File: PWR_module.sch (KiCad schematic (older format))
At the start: 16 parts, among them P14 CONN_01X02, P15 FUSE, T1 TRANSFO, U1 SPX2920M3-3.3, U7 SPX2920M3-3.3, U8 SPX2920M3-3.3, U9 SPX2920M3-3.3

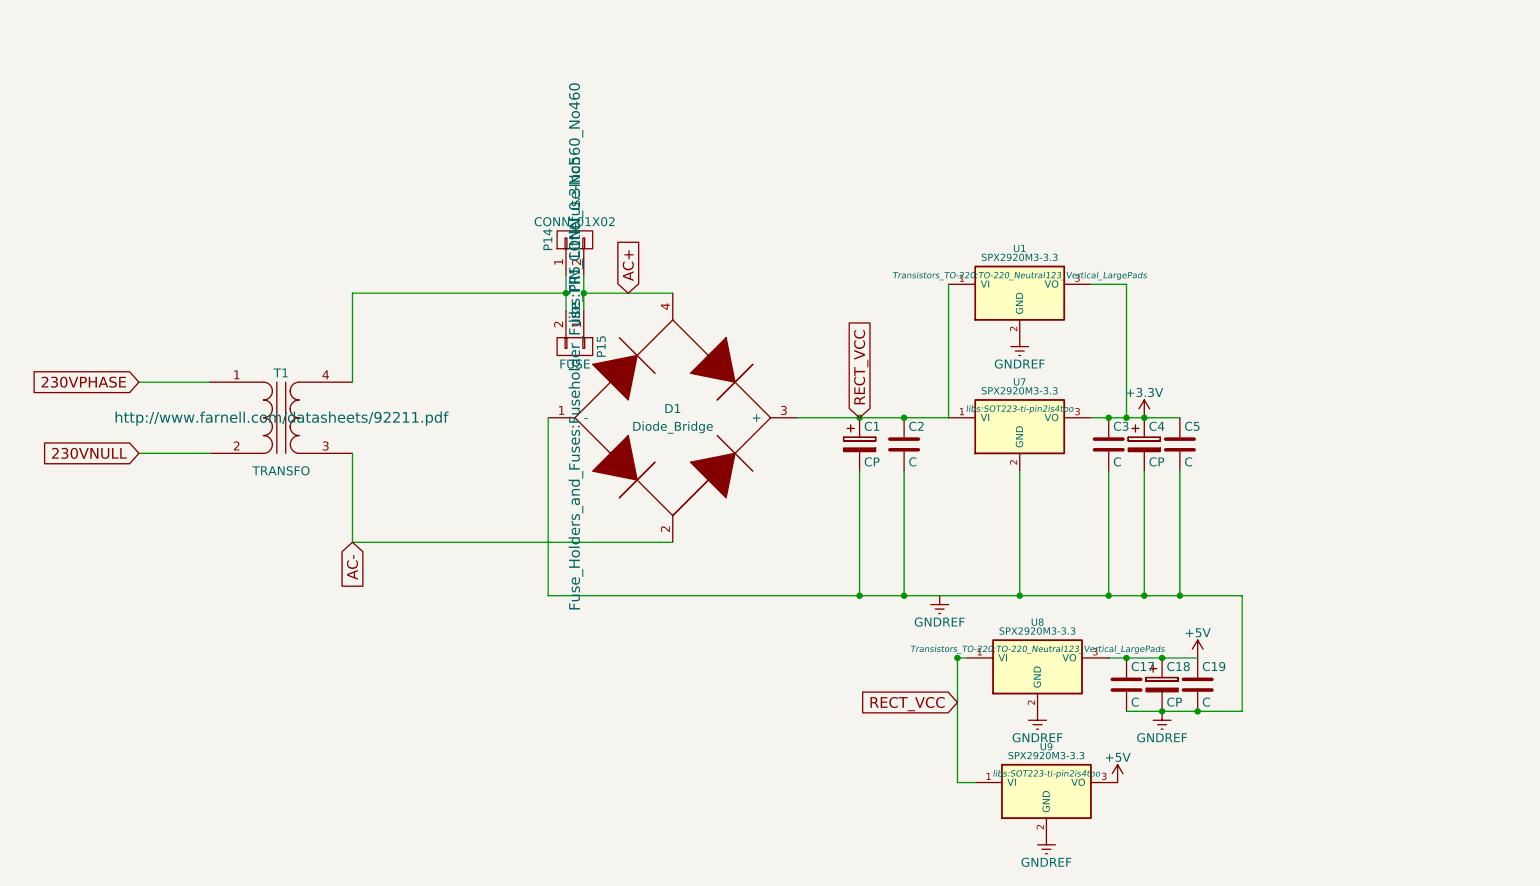
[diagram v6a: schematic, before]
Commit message: new layout, added psu
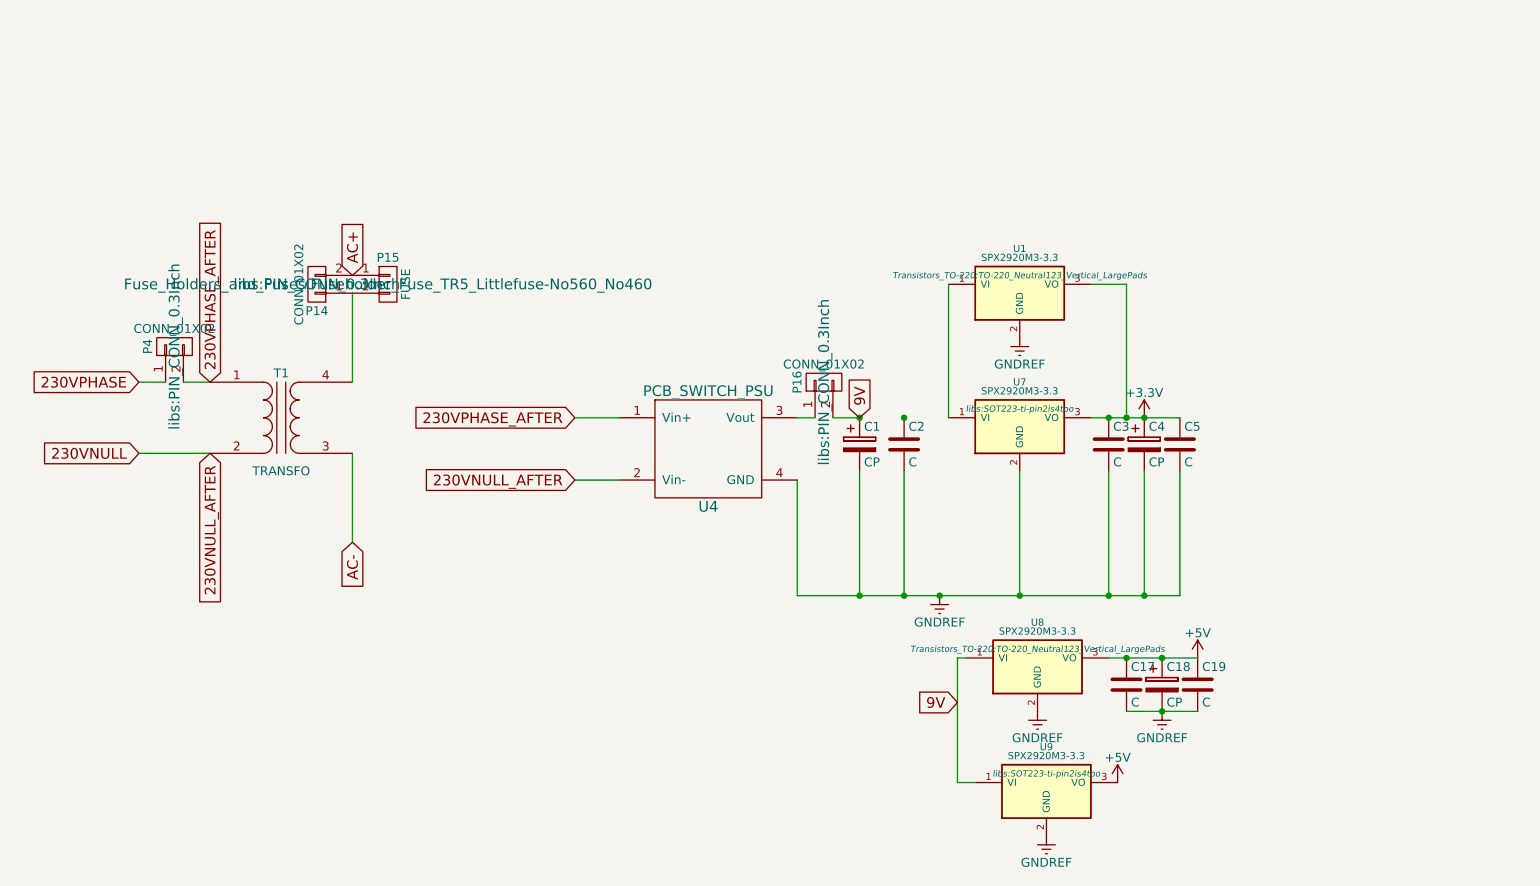
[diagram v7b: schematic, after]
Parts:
- removed D1: Diode_Bridge, libs:rb1a_mb6sbridge, symbol Diode_Bridge-RESCUE-viztisztito
- added P16, P4: CONN_01X02, libs:PIN_CONN_0.3Inch, symbol CONN_01X02
- added U4: PCB_SWITCH_PSU, libs:VTX_214_010_109_AC_DC_PCB_Mount_Power_Supply, symbol PCB_SWITCH_PSU
- C1: footprint Capacitors_Elko_ThroughHole:Elko_vert_31.5x16mm_RM7.5 -> Capacitors_ThroughHole:C_Radial_D16_L31.5_P7.5
- C18, C4: footprint Capacitors_Elko_ThroughHole:Elko_vert_31.5x16mm_RM7.5 -> Capacitors_ThroughHole:C_Radial_D16_L30_P7.5
- T1: footprint libs:MYRRA_44266 -> libs:MYRRA44050_IsolationTransformer
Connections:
- net 230VNULL: now also U4.2 (Vin-)
- net 230VPHASE: now also P4.1 (P1); no longer T1.1 (AA)
- net GNDREF: now also U4.4 (GND)
- net RECT_VCC renamed 9V
- net 9V: now also P16.2 (P2); no longer C2.1, U1.1 (VI), U7.1 (VI)
- new net: U1.1 (VI), U7.1 (VI)
- new net: P16.1 (P1), U4.3 (Vout)
- new net 230VPHASE_AFTER: P4.2 (P2), T1.1 (AA), U4.1 (Vin+)
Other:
- moved on the sheet: P14, P15
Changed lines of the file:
@@
 LIBS:contrib
 LIBS:valves
-LIBS:mylib
+LIBS:analog_devices
+LIBS:libs
 LIBS:viztisztito-cache
 EELAYER 25 0
@@
 F 0 "T1" H 3150 3100 50  0000 C CNN
 F 1 "TRANSFO" H 3150 2550 50  0000 C CNN
-F 2 "libs:MYRRA_44266" H 3150 2850 60  0001 C CNN
-F 3 "http://www.farnell.com/datasheets/92211.pdf" H 3150 2850 60  0000 C CNN
+F 2 "libs:MYRRA44050_IsolationTransformer" H 3150 2850 60  0001 C CNN
+F 3 "http://hu.farnell.com/myrra/44050/transformer-9v-1va/dp/1689042" H 3150 2850 60  0001 C CNN
 	1    3150 2850
 	1    0    0    -1
@@
 F 0 "C1" H 6425 3100 50  0000 L CNN
 F 1 "CP" H 6425 2900 50  0000 L CNN
-F 2 "Capacitors_Elko_ThroughHole:Elko_vert_31.5x16mm_RM7.5" H 6438 2850 30  0001 C CNN
+F 2 "Capacitors_ThroughHole:C_Radial_D16_L31.5_P7.5" H 6438 2850 30  0001 C CNN
 F 3 "" H 6400 3000 60  0000 C CNN
 	1    6400 3000
@@
 F 0 "C4" H 8025 3100 50  0000 L CNN
 F 1 "CP" H 8025 2900 50  0000 L CNN
-F 2 "Capacitors_Elko_ThroughHole:Elko_vert_31.5x16mm_RM7.5" H 8038 2850 30  0001 C CNN
+F 2 "Capacitors_ThroughHole:C_Radial_D16_L30_P7.5" H 8038 2850 30  0001 C CNN
 F 3 "" H 8000 3000 60  0000 C CNN
 	1    8000 3000
@@
 	1    0    0    -1
 $EndComp
-Text GLabel 5100 2150 1    60   Input ~ 0
+Text GLabel 3550 2050 1    60   Input ~ 0
 AC+
 Text GLabel 3550 3550 3    60   Input ~ 0
@@
 $EndComp
 Text GLabel 6400 2850 1    60   Input ~ 0
-RECT_VCC
+9V
 $Comp
 L GNDREF #PWR012
@@
 F 0 "C18" H 8125 4450 50  0000 L CNN
 F 1 "CP" H 8125 4250 50  0000 L CNN
-F 2 "Capacitors_Elko_ThroughHole:Elko_vert_31.5x16mm_RM7.5" H 8138 4200 30  0001 C CNN
+F 2 "Capacitors_ThroughHole:C_Radial_D16_L30_P7.5" H 8138 4200 30  0001 C CNN
 F 3 "" H 8100 4350 60  0000 C CNN
 	1    8100 4350
@@
 	1    0    0    -1
 $EndComp
+Wire Wire Line
+	2350 3050 2750 3050
+Wire Wire Line
+	3550 2650 3550 2150
+Wire Wire Line
+	3550 3550 3550 3050
+Wire Wire Line
+	6400 3850 6400 3150
+Wire Wire Line
+	6650 3850 6650 3150
+Connection ~ 6400 2850
+Wire Wire Line
+	7300 3850 7300 3150
+Connection ~ 6650 2850
+Wire Wire Line
+	7700 2850 8200 2850
+Connection ~ 7800 2850
+Connection ~ 8000 2850
+Wire Wire Line
+	8200 3850 8200 3150
+Wire Wire Line
+	8000 3850 8000 3150
+Wire Wire Line
+	7800 3850 7800 3150
+Wire Wire Line
+	6900 2850 6900 2100
+Wire Wire Line
+	7700 2100 7900 2100
+Wire Wire Line
+	7900 2100 7900 2850
+Connection ~ 7900 2850
+Wire Wire Line
+	6950 4200 7000 4200
+Wire Wire Line
+	7800 4200 8300 4200
+Connection ~ 7900 4200
+Connection ~ 8100 4200
+Wire Wire Line
+	6950 4900 7050 4900
+Text GLabel 6950 4450 0    60   Input ~ 0
+9V
+Text GLabel 2350 2650 0    60   Input ~ 0
+230VPHASE
+Text GLabel 2350 3050 0    60   Input ~ 0
+230VNULL
+$Comp
+L CONN_01X02 P14
+U 1 1 5630FFA8
+P 3350 2100
+F 0 "P14" H 3350 2250 50  0000 C CNN
+F 1 "CONN_01X02" V 3450 2100 50  0000 C CNN
+F 2 "libs:PIN_CONN_0.3Inch" H 3350 2100 60  0000 C CNN
+F 3 "" H 3350 2100 60  0000 C CNN
+	1    3350 2100
+	-1   0    0    1
+$EndComp
+$Comp
+L CONN_01X02 P15
+U 1 1 5634C69D
+P 3750 2100
+F 0 "P15" H 3750 2250 50  0000 C CNN
+F 1 "FUSE" V 3850 2100 50  0000 C CNN
+F 2 "Fuse_Holders_and_Fuses:Fuseholder_Fuse_TR5_Littlefuse-No560_No460" H 3750 2100 60  0000 C CNN
+F 3 "" H 3750 2100 60  0000 C CNN
+	1    3750 2100
+	1    0    0    -1
+$EndComp
+$Comp
+L CONN_01X02 P4
+U 1 1 569EE014
+P 2550 2450
+F 0 "P4" H 2550 2600 50  0000 C CNN
+F 1 "CONN_01X02" V 2650 2450 50  0000 C CNN
+F 2 "libs:PIN_CONN_0.3Inch" H 2550 2450 60  0000 C CNN
+F 3 "" H 2550 2450 60  0000 C CNN
+	1    2550 2450
+	0    -1   -1   0
+$EndComp
+Wire Wire Line
+	2350 2650 2500 2650
+Wire Wire Line
+	2600 2650 2750 2650
+$Comp
+L PCB_SWITCH_PSU U4
+U 1 1 56BF21F3
+P 5550 3050
+F 0 "U4" H 5550 2750 60  0000 C CNN
+F 1 "PCB_SWITCH_PSU" H 5550 3400 60  0000 C CNN
+F 2 "libs:VTX_214_010_109_AC_DC_PCB_Mount_Power_Supply" H 5550 3050 60  0001 C CNN
+F 3 "http://hu.farnell.com/vigortronix/vtx-214-010-109/ac-dc-conv-fixed-1-o-p-10w-9v/dp/2401053" H 5550 3050 60  0001 C CNN
+	1    5550 3050
+	1    0    0    -1
+$EndComp
+Text GLabel 4800 2850 0    60   Input ~ 0
+230VPHASE_AFTER
+Text GLabel 4800 3200 0    60   Input ~ 0
+230VNULL_AFTER
+Wire Wire Line
+	4800 2850 5050 2850
+Wire Wire Line
+	4800 3200 5050 3200
+Wire Wire Line
+	6050 3200 6050 3850
+Wire Wire Line
+	6050 3850 8200 3850
+Connection ~ 6400 3850
+Connection ~ 6650 3850
+Connection ~ 6850 3850
+Connection ~ 7300 3850
+Connection ~ 7800 3850
+Connection ~ 8000 3850
+Wire Wire Line
+	7900 4500 8300 4500
+Connection ~ 8100 4500
 $Comp
 L SPX2920M3-3.3 U8
@@
 $EndComp
 Wire Wire Line
-	2350 3050 2750 3050
-Wire Wire Line
-	2750 2650 2350 2650
-Wire Wire Line
-	3550 2650 3550 2150
-Wire Wire Line
-	5350 3550 3550 3550
-Wire Wire Line
-	3550 3550 3550 3050
-Wire Wire Line
-	4650 2850 4650 3850
-Wire Wire Line
-	6400 3850 6400 3150
-Wire Wire Line
-	6650 3850 6650 3150
-Connection ~ 6400 3850
-Connection ~ 6400 2850
-Wire Wire Line
-	7300 3850 7300 3150
-Connection ~ 6650 3850
-Connection ~ 6650 2850
-Wire Wire Line
-	7700 2850 8200 2850
-Connection ~ 7800 2850
-Connection ~ 8000 2850
-Wire Wire Line
-	8200 3850 8200 3150
-Connection ~ 7300 3850
-Wire Wire Line
-	8000 3850 8000 3150
-Connection ~ 8000 3850
-Wire Wire Line
-	7800 3850 7800 3150
-Connection ~ 7800 3850
-Connection ~ 8200 3850
-Wire Wire Line
-	4650 3850 8550 3850
-Wire Wire Line
-	6900 2850 6900 2100
-Wire Wire Line
-	7700 2100 7900 2100
-Wire Wire Line
-	7900 2100 7900 2850
-Connection ~ 7900 2850
-Wire Wire Line
 	6950 4200 6950 4900
-Wire Wire Line
-	6950 4200 7000 4200
-Wire Wire Line
-	7800 4200 8300 4200
-Connection ~ 7900 4200
-Connection ~ 8100 4200
-Wire Wire Line
-	7900 4500 8550 4500
-Connection ~ 8100 4500
-Wire Wire Line
-	6950 4900 7050 4900
-Connection ~ 6950 4200
-Wire Wire Line
-	8550 4500 8550 3850
-Connection ~ 8300 4500
-Text GLabel 6950 4450 0    60   Input ~ 0
-RECT_VCC
-Text GLabel 2350 2650 0    60   Input ~ 0
-230VPHASE
-Text GLabel 2350 3050 0    60   Input ~ 0
-230VNULL
-$Comp
-L CONN_01X02 P14
-U 1 1 5630FFA8
-P 4800 1850
-F 0 "P14" H 4800 2000 50  0000 C CNN
-F 1 "CONN_01X02" V 4900 1850 50  0000 C CNN
-F 2 "libs:PIN_CONN_0.3Inch" H 4800 1850 60  0000 C CNN
-F 3 "" H 4800 1850 60  0000 C CNN
-	1    4800 1850
+$Comp
+L CONN_01X02 P16
+U 1 1 56CE1D02
+P 6200 2650
+F 0 "P16" H 6200 2800 50  0000 C CNN
+F 1 "CONN_01X02" V 6300 2650 50  0000 C CNN
+F 2 "libs:PIN_CONN_0.3Inch" H 6200 2650 60  0000 C CNN
+F 3 "" H 6200 2650 60  0000 C CNN
+	1    6200 2650
 	0    -1   -1   0
 $EndComp
 Wire Wire Line
-	6050 2850 6900 2850
-$Comp
-L Diode_Bridge-RESCUE-viztisztito D1
-U 1 1 5614DBFC
-P 5350 2850
-F 0 "D1" H 5350 2900 50  0000 C CNN
-F 1 "Diode_Bridge" H 5350 2800 50  0000 C CNN
-F 2 "libs:rb1a_mb6sbridge" H 5350 2850 60  0001 C CNN
-F 3 "" H 5350 2850 60  0000 C CNN
-	1    5350 2850
-	1    0    0    -1
-$EndComp
-Wire Wire Line
-	4750 2050 4750 2250
-Connection ~ 4750 2150
-Wire Wire Line
-	4850 2050 4850 2250
-Connection ~ 4850 2150
-Wire Wire Line
-	4850 2150 5350 2150
-Wire Wire Line
-	3550 2150 4750 2150
-$Comp
-L CONN_01X02 P15
-U 1 1 5634C69D
-P 4800 2450
-F 0 "P15" H 4800 2600 50  0000 C CNN
-F 1 "FUSE" V 4900 2450 50  0000 C CNN
-F 2 "Fuse_Holders_and_Fuses:Fuseholder_Fuse_TR5_Littlefuse-No560_No460" H 4800 2450 60  0000 C CNN
-F 3 "" H 4800 2450 60  0000 C CNN
-	1    4800 2450
-	0    1    1    0
-$EndComp
+	6050 2850 6150 2850
+Wire Wire Line
+	6250 2850 6400 2850
+Text GLabel 2750 2650 1    60   Input ~ 0
+230VPHASE_AFTER
+Text GLabel 2750 3050 3    60   Input ~ 0
+230VNULL_AFTER
 $EndSCHEMATC

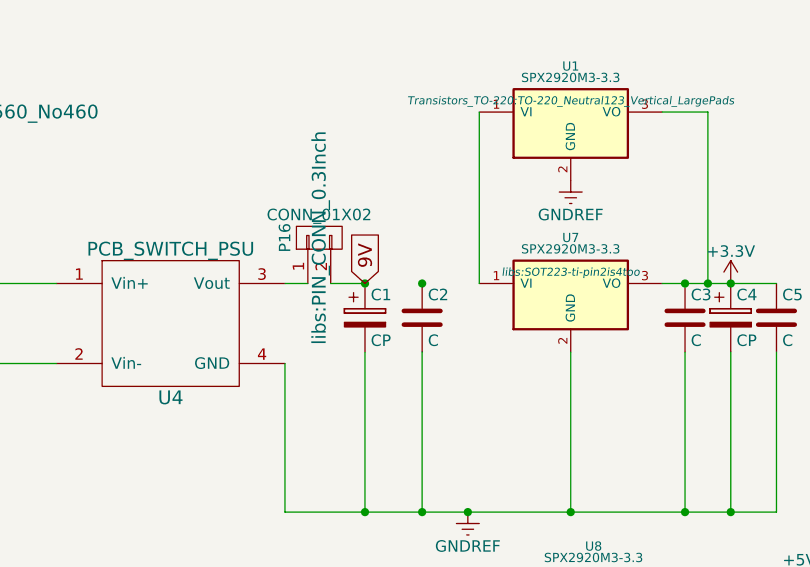
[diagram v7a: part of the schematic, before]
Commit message: checked gerbers, possible problems in edge cuts?
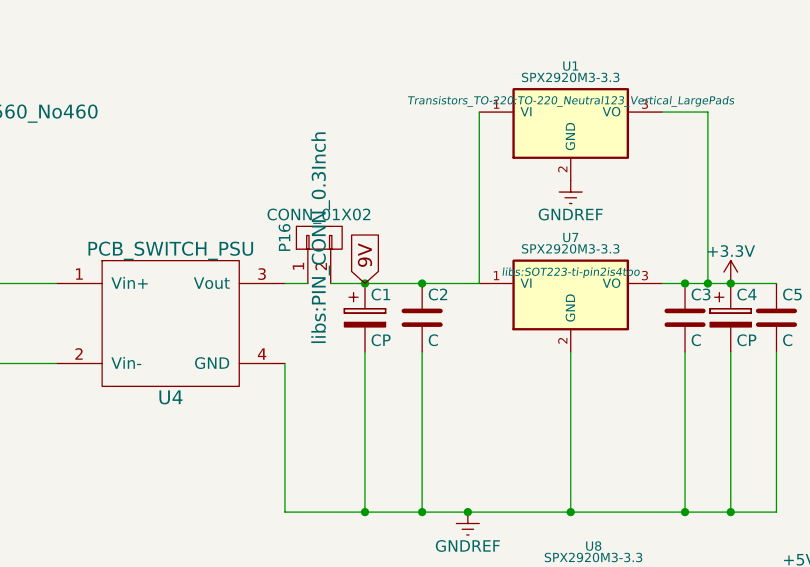
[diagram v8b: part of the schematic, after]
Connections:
- net 9V: now also C2.1, U1.1 (VI), U7.1 (VI)
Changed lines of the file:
@@
 	6050 2850 6150 2850
 Wire Wire Line
-	6250 2850 6400 2850
+	6250 2850 6900 2850
 Text GLabel 2750 2650 1    60   Input ~ 0
 230VPHASE_AFTER
